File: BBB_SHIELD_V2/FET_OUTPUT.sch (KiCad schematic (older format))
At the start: 4 parts, among them U2 TC4432

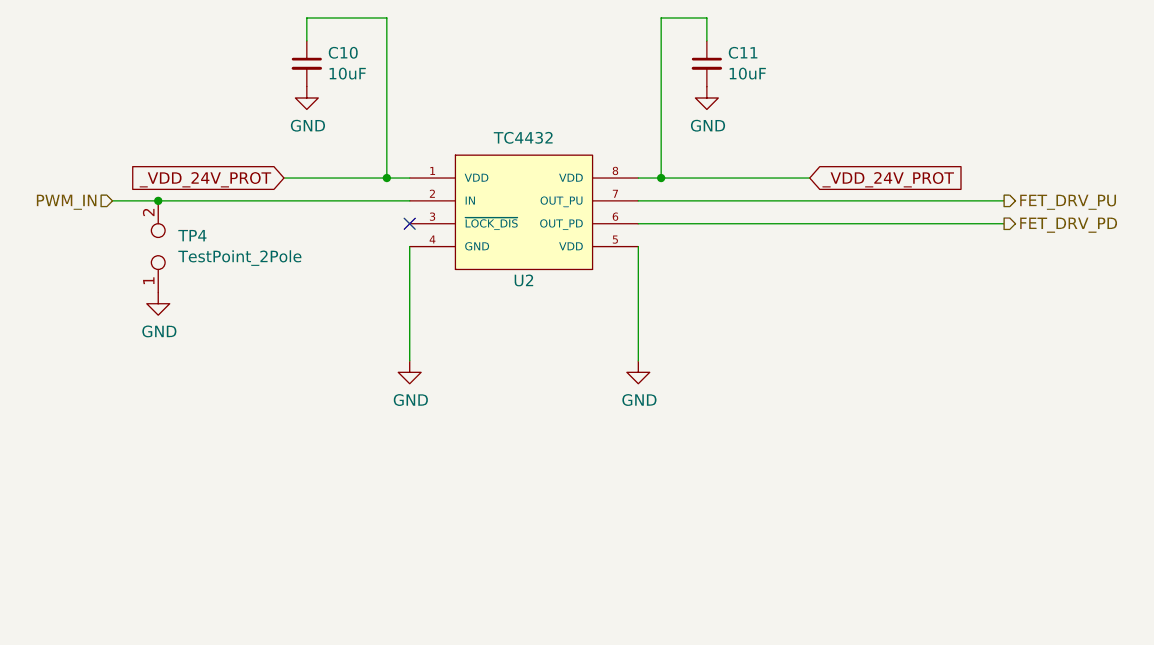
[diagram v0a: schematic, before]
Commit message: Changed to high-side switching of power supply to boards.  Changed footprints to SOIC.  Misc other changes.
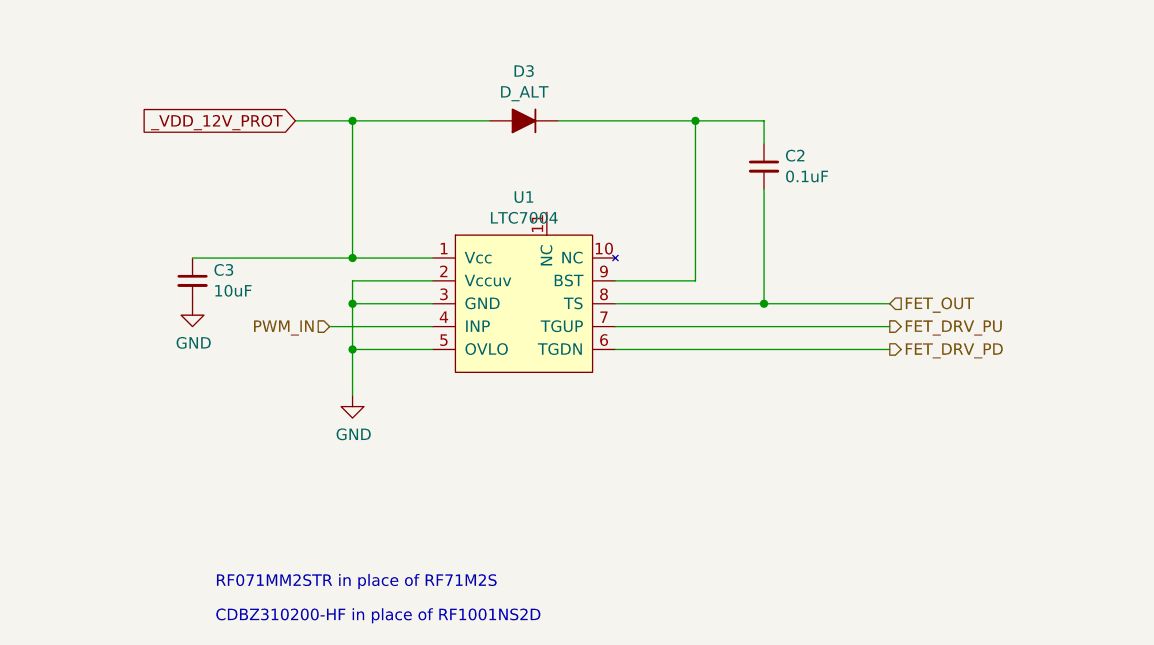
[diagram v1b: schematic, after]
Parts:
- removed C11: 10uF, Capacitor_SMD:C_1206_3216Metric, symbol Device:C_Small
- removed TP4: TestPoint_2Pole, Connector_PinHeader_1.27mm:PinHeader_1x02_P1.27mm_Vertical, symbol Connector:TestPoint_2Pole
- removed U2: TC4432, Package_SO:SOIC-8_3.9x4.9mm_P1.27mm, symbol CUSTOM_COMPONENTS:TC4432
- added C2: 0.1uF, Capacitor_SMD:C_0805_2012Metric, symbol Device:C_Small
- added D3: D_ALT, Diode_SMD:D_SOD-123F, symbol Device:D_ALT
- added U1: LTC7004, CUSTOM_FOOTPRINTS:MSOP-10, symbol CUSTOM_COMPONENTS:LTC7004
- C3: renamed from C10; DKPN (none) -> 1276-6767-1-ND; MFG (none) -> SAMSUNG; MFGPN (none) -> CL31B106KBHNNNE; NOTES (none) -> CT, VER 2018-11-25; TEMPCO (none) -> X7R; VOLTAGE (none) -> 50
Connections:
- net FET_DRV_PD: now also U1.6 (TGDN)
- net FET_DRV_PU: now also U1.7 (TGUP)
- net GND: now also U1.2 (Vccuv), U1.3 (GND), U1.5 (OVLO)
- net PWM_IN: now also U1.4 (INP)
- net _VDD_24V_PROT renamed _VDD_12V_PROT
- net _VDD_12V_PROT: now also D3.2 (A), U1.1 (Vcc)
- new net: C2.1, D3.1 (K), U1.9 (BST)
- new net FET_OUT: C2.2, U1.8 (TS)
- no-connect marks 1 -> 0
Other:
- note added: "CDBZ310200-HF in place of RF1001NS2D"
- note added: "‎RF071MM2STR‎ in place of RF71M2S"
- moved on the sheet: C3
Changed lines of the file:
@@
 $Descr A4 11693 8268
 encoding utf-8
-Sheet 4 11
+Sheet 3 12
 Title ""
 Date ""
@@
 $EndDescr
 $Comp
-L CUSTOM_COMPONENTS:TC4432 U2
-U 1 1 5B9E7A80
-P 5850 3200
-F 0 "U2" H 5850 2900 50  0000 C CNN
-F 1 "TC4432" H 5850 3524 50  0000 C CNN
-F 2 "Package_SO:SOIC-8_3.9x4.9mm_P1.27mm" H 5450 3300 50  0001 C CNN
-F 3 "" H 5450 3300 50  0001 C CNN
-	1    5850 3200
+L Device:C_Small C3
+U 1 1 5B9E8A85
+P 4400 3500
+F 0 "C3" H 4492 3546 50  0000 L CNN
+F 1 "10uF" H 4492 3455 50  0000 L CNN
+F 2 "Capacitor_SMD:C_1206_3216Metric" H 4400 3500 50  0001 C CNN
+F 3 "" H 4400 3500 50  0001 C CNN
+F 4 "1276-6767-1-ND" H -500 950 50  0001 C CNN "DKPN"
+F 5 "SAMSUNG" H -500 950 50  0001 C CNN "MFG"
+F 6 "CL31B106KBHNNNE" H -500 950 50  0001 C CNN "MFGPN"
+F 7 "X7R" H -500 950 50  0001 C CNN "TEMPCO"
+F 8 "50" H -500 950 50  0001 C CNN "VOLTAGE"
+F 9 "CT, VER 2018-11-25" H -500 950 50  0001 C CNN "NOTES"
+	1    4400 3500
 	1    0    0    -1
 $EndComp
-Text GLabel 4800 3050 0    50   Input ~ 0
-_VDD_24V_PROT
-Text GLabel 7100 3050 2    50   Input ~ 0
-_VDD_24V_PROT
+Text HLabel 5000 3700 0    50   Input ~ 0
+PWM_IN
+$Comp
+L power:GND #PWR04
+U 1 1 5B9E9DF1
+P 4400 3600
+F 0 "#PWR04" H 4400 3350 50  0001 C CNN
+F 1 "GND" H 4405 3427 50  0000 C CNN
+F 2 "" H 4400 3600 50  0001 C CNN
+F 3 "" H 4400 3600 50  0001 C CNN
+	1    4400 3600
+	1    0    0    -1
+$EndComp
+Text HLabel 7450 3700 2    50   Output ~ 0
+FET_DRV_PU
+Text HLabel 7450 3800 2    50   Output ~ 0
+FET_DRV_PD
 Wire Wire Line
-	7100 3050 6450 3050
+	7450 3700 6250 3700
 Wire Wire Line
-	5350 3050 5250 3050
-Wire Wire Line
-	5250 3050 5250 2350
-Connection ~ 5250 3050
-Wire Wire Line
-	5250 3050 4800 3050
-Wire Wire Line
-	6450 3050 6450 2350
-Wire Wire Line
-	6450 2350 6650 2350
-Connection ~ 6450 3050
-Wire Wire Line
-	6450 3050 6350 3050
+	7450 3800 6250 3800
+Text Notes 4500 4850 0    50   ~ 0
+‎RF071MM2STR‎ in place of RF71M2S
+Text Notes 4500 5000 0    50   ~ 0
+CDBZ310200-HF in place of RF1001NS2D
 $Comp
-L Device:C_Small C10
-U 1 1 5B9E8A85
-P 4900 2550
-F 0 "C10" H 4992 2596 50  0000 L CNN
-F 1 "10uF" H 4992 2505 50  0000 L CNN
-F 2 "Capacitor_SMD:C_1206_3216Metric" H 4900 2550 50  0001 C CNN
-F 3 "~" H 4900 2550 50  0001 C CNN
-	1    4900 2550
+L CUSTOM_COMPONENTS:LTC7004 U1
+U 1 1 5C317C6E
+P 5450 3450
+F 0 "U1" H 5850 3765 50  0000 C CNN
+F 1 "LTC7004" H 5850 3674 50  0000 C CNN
+F 2 "CUSTOM_FOOTPRINTS:MSOP-10" H 5450 3450 50  0001 C CNN
+F 3 "" H 5450 3450 50  0001 C CNN
+F 4 "LTC7004IMSE#PBF-ND" H 5450 3450 50  0001 C CNN "DKPN"
+F 5 "LTC7004IMSE#PBF" H 5450 3450 50  0001 C CNN "MFGPN"
+	1    5450 3450
 	1    0    0    -1
 $EndComp
 $Comp
-L Device:C_Small C11
-U 1 1 5B9E8B0B
-P 6650 2550
-F 0 "C11" H 6558 2596 50  0000 R CNN
-F 1 "10uF" H 6558 2505 50  0000 R CNN
-F 2 "Capacitor_SMD:C_1206_3216Metric" H 6650 2550 50  0001 C CNN
-F 3 "~" H 6650 2550 50  0001 C CNN
-	1    6650 2550
-	-1   0    0    -1
+L Device:D_ALT D3
+U 1 1 5CF18E5C
+P 5850 2800
+F 0 "D3" H 5850 2584 50  0000 C CNN
+F 1 "D_ALT" H 5850 2675 50  0000 C CNN
+F 2 "Diode_SMD:D_SOD-123F" H 5850 2800 50  0001 C CNN
+F 3 "~" H 5850 2800 50  0001 C CNN
+F 4 "RF071MM2SCT-ND" H 5850 2800 50  0001 C CNN "DKPN"
+F 5 "RF071MM2STR" H 5850 2800 50  0001 C CNN "MFGPN"
+	1    5850 2800
+	-1   0    0    1
 $EndComp
 Wire Wire Line
-	4900 2450 4900 2350
+	5100 3400 5100 2800
 Wire Wire Line
-	4900 2350 5250 2350
+	5100 2800 5700 2800
 Wire Wire Line
-	6650 2450 6650 2350
+	6000 2800 6600 2800
+Wire Wire Line
+	6600 2800 6600 3500
+Wire Wire Line
+	6600 3500 6250 3500
 $Comp
-L power:GND #PWR011
-U 1 1 5B9E902F
-P 6650 2650
-F 0 "#PWR011" H 6650 2400 50  0001 C CNN
-F 1 "GND" H 6655 2477 50  0000 C CNN
-F 2 "" H 6650 2650 50  0001 C CNN
-F 3 "" H 6650 2650 50  0001 C CNN
-	1    6650 2650
+L Device:C_Small C2
+U 1 1 5CF198EC
+P 6900 3000
+F 0 "C2" H 6992 3046 50  0000 L CNN
+F 1 "0.1uF" H 6992 2955 50  0000 L CNN
+F 2 "Capacitor_SMD:C_0805_2012Metric" H 6900 3000 50  0001 C CNN
+F 3 "~" H 6900 3000 50  0001 C CNN
+	1    6900 3000
 	1    0    0    -1
 $EndComp
+Wire Wire Line
+	6250 3600 6900 3600
+Wire Wire Line
+	6900 3600 6900 3100
+Wire Wire Line
+	6900 2900 6900 2800
+Wire Wire Line
+	6900 2800 6600 2800
+Connection ~ 6600 2800
+Text HLabel 7450 3600 2    50   Input ~ 0
+FET_OUT
+Connection ~ 6900 3600
+Wire Wire Line
+	5450 3800 5100 3800
+Wire Wire Line
+	5100 3800 5100 3600
+Wire Wire Line
+	5100 3600 5450 3600
+Wire Wire Line
+	5450 3500 5100 3500
+Wire Wire Line
+	5100 3500 5100 3600
+Connection ~ 5100 3600
+Wire Wire Line
+	5100 3800 5100 4000
+Connection ~ 5100 3800
 $Comp
-L power:GND #PWR08
-U 1 1 5B9E9060
-P 4900 2650
-F 0 "#PWR08" H 4900 2400 50  0001 C CNN
-F 1 "GND" H 4905 2477 50  0000 C CNN
-F 2 "" H 4900 2650 50  0001 C CNN
-F 3 "" H 4900 2650 50  0001 C CNN
-	1    4900 2650
+L power:GND #PWR05
+U 1 1 5CF1E951
+P 5100 4000
+F 0 "#PWR05" H 5100 3750 50  0001 C CNN
+F 1 "GND" H 5105 3827 50  0000 C CNN
+F 2 "" H 5100 4000 50  0001 C CNN
+F 3 "" H 5100 4000 50  0001 C CNN
+	1    5100 4000
 	1    0    0    -1
 $EndComp
-Text HLabel 4050 3150 0    50   Input ~ 0
-PWM_IN
+Text GLabel 4850 2800 0    50   Input ~ 0
+_VDD_12V_PROT
 Wire Wire Line
-	4050 3150 4250 3150
-NoConn ~ 5350 3250
+	4850 2800 5100 2800
+Connection ~ 5100 2800
+Connection ~ 5100 3400
 Wire Wire Line
-	6350 3350 6350 3850
+	5100 3400 5450 3400
 Wire Wire Line
-	5350 3350 5350 3850
-$Comp
-L power:GND #PWR010
-U 1 1 5B9E9DF1
-P 6350 3850
-F 0 "#PWR010" H 6350 3600 50  0001 C CNN
-F 1 "GND" H 6355 3677 50  0000 C CNN
-F 2 "" H 6350 3850 50  0001 C CNN
-F 3 "" H 6350 3850 50  0001 C CNN
-	1    6350 3850
-	1    0    0    -1
-$EndComp
-$Comp
-L power:GND #PWR09
-U 1 1 5B9E9E22
-P 5350 3850
-F 0 "#PWR09" H 5350 3600 50  0001 C CNN
-F 1 "GND" H 5355 3677 50  0000 C CNN
-F 2 "" H 5350 3850 50  0001 C CNN
-F 3 "" H 5350 3850 50  0001 C CNN
-	1    5350 3850
-	1    0    0    -1
-$EndComp
-Text HLabel 7950 3150 2    50   Output ~ 0
-FET_DRV_PU
-Text HLabel 7950 3250 2    50   Output ~ 0
-FET_DRV_PD
+	4400 3400 5100 3400
 Wire Wire Line
-	7950 3150 6350 3150
+	6900 3600 7450 3600
 Wire Wire Line
-	7950 3250 6350 3250
-$Comp
-L Connector:TestPoint_2Pole TP4
-U 1 1 5BD67BDA
-P 4250 3350
-F 0 "TP4" V 4296 3262 50  0000 R CNN
-F 1 "TestPoint_2Pole" V 4205 3262 50  0000 R CNN
-F 2 "Connector_PinHeader_1.27mm:PinHeader_1x02_P1.27mm_Vertical" H 4250 3350 50  0001 C CNN
-F 3 "~" H 4250 3350 50  0001 C CNN
-	1    4250 3350
-	0    -1   -1   0
-$EndComp
-Connection ~ 4250 3150
-Wire Wire Line
-	4250 3150 5350 3150
-$Comp
-L power:GND #PWR07
-U 1 1 5BD67C73
-P 4250 3550
-F 0 "#PWR07" H 4250 3300 50  0001 C CNN
-F 1 "GND" H 4255 3377 50  0000 C CNN
-F 2 "" H 4250 3550 50  0001 C CNN
-F 3 "" H 4250 3550 50  0001 C CNN
-	1    4250 3550
-	1    0    0    -1
-$EndComp
+	5000 3700 5450 3700
 $EndSCHEMATC

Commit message: Schematic cleanup and refinement.
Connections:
- net GND: now also U1.11 (NC)
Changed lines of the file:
@@
 Wire Wire Line
 	5000 3700 5450 3700
+Wire Wire Line
+	5950 3200 5950 3000
+Wire Wire Line
+	5950 3000 6450 3000
+Wire Wire Line
+	6450 3000 6450 3050
+$Comp
+L power:GND #PWR0101
+U 1 1 5D153AE4
+P 6450 3050
+F 0 "#PWR0101" H 6450 2800 50  0001 C CNN
+F 1 "GND" H 6455 2877 50  0000 C CNN
+F 2 "" H 6450 3050 50  0001 C CNN
+F 3 "" H 6450 3050 50  0001 C CNN
+	1    6450 3050
+	1    0    0    -1
+$EndComp
 $EndSCHEMATC

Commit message: Rev 2 problem fixes.
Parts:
- C2: value 0.1uF -> 1uF; DKPN (none) -> 1276-1003-1-ND; MFG (none) -> SAMSUNG; MFGPN (none) -> CL21B104KBCNNNC; NOTES (none) -> VER,2019-07-17,REEL; TEMPCO (none) -> X7R; VOLTAGE (none) -> 50
- C3: NOTES CT, VER 2018-11-25 -> VER,2019-07-17,CT
- D3: NOTES (none) -> VER,2019-07-15,CT
- U1: NOTES (none) -> VER,2019-07-16,CT
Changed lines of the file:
@@
 F 7 "X7R" H -500 950 50  0001 C CNN "TEMPCO"
 F 8 "50" H -500 950 50  0001 C CNN "VOLTAGE"
-F 9 "CT, VER 2018-11-25" H -500 950 50  0001 C CNN "NOTES"
+F 9 "VER,2019-07-17,CT" H -500 950 50  0001 C CNN "NOTES"
 	1    4400 3500
 	1    0    0    -1
@@
 F 4 "LTC7004IMSE#PBF-ND" H 5450 3450 50  0001 C CNN "DKPN"
 F 5 "LTC7004IMSE#PBF" H 5450 3450 50  0001 C CNN "MFGPN"
+F 6 "VER,2019-07-16,CT" H 0   0   50  0001 C CNN "NOTES"
 	1    5450 3450
 	1    0    0    -1
@@
 F 4 "RF071MM2SCT-ND" H 5850 2800 50  0001 C CNN "DKPN"
 F 5 "RF071MM2STR" H 5850 2800 50  0001 C CNN "MFGPN"
+F 6 "VER,2019-07-15,CT" H 0   0   50  0001 C CNN "NOTES"
 	1    5850 2800
 	-1   0    0    1
@@
 P 6900 3000
 F 0 "C2" H 6992 3046 50  0000 L CNN
-F 1 "0.1uF" H 6992 2955 50  0000 L CNN
+F 1 "1uF" H 6992 2955 50  0000 L CNN
 F 2 "Capacitor_SMD:C_0805_2012Metric" H 6900 3000 50  0001 C CNN
 F 3 "~" H 6900 3000 50  0001 C CNN
+F 4 "1276-1003-1-ND " H 0   0   50  0001 C CNN "DKPN"
+F 5 "SAMSUNG" H 0   0   50  0001 C CNN "MFG"
+F 6 "CL21B104KBCNNNC" H 0   0   50  0001 C CNN "MFGPN"
+F 7 "X7R" H 0   0   50  0001 C CNN "TEMPCO"
+F 8 "50" H 0   0   50  0001 C CNN "VOLTAGE"
+F 9 "VER,2019-07-17,REEL" H 0   0   50  0001 C CNN "NOTES"
 	1    6900 3000
 	1    0    0    -1
